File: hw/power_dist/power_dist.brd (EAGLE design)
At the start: 70 x 45 mm, 57 parts, among them J1 JST-ZH6SMT_VERT, J2 JST-PH4SMT_VERT, P1 XT30P, P2 XT30P, P3 XT30P, P4 XT30P, P5 XT30P, P6 XT30P, P7 XT90PW-M, Q1 TPH1R204PL, Q2 TPH1R204PL, Q3 TPH1R204PL, U1 ZXTR2012Z, U2 MAX150628TDFN, U3 STM32G474CEU6, U4 MIC4416, U5 MIC4416, U6 TCAN334G

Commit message: WIP of power_dist r4
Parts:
- removed D12, D3V3, DG, DI: PAD24AWG_PAD, precharge:24AWG_PAD
- removed D2: (no value), mfleds:LED0603
- removed D3: (no value), imu_junction:DO-214AB
- removed Q1, Q2, Q3: TPH1R204PL, imu_junction:SOP_ADVANCE
- added CR1: SMBJ51CA-E3/52, power_dist:DIODE_DO-214AC
- added MOSFET1, MOSFET2, MOSFET3: PSMN4R8-100BSEJ, power_dist:D2PAK_SOT404_NEX
- added R11, R12: 10k, mfpassives:R0603
- added R13: 15k 1%, mfpassives:R0603
- added U$5: JST-PH5VERT, power_dist:JST_B5B_PH-SM4-TB(LF)(SN)
- added U7: MF-DSC-SOT233-BSS138, mfdiscretesemi:SOT-23-3
- C1: value 1uF 50V -> 1uF
- C10, C11, C12, C13, C14, C3, C4: device mfpassives:C0402 -> mfpassives:C0603
- C5: value 0.1uF -> 0.01uF; device mfpassives:C0402 -> mfpassives:C0603
- C6: value 0.1uF -> 0.082uF; device mfpassives:C0402 -> mfpassives:C0603
- C7: value 10uF 50V -> 1uF; device mfpassives:C1206 -> mfpassives:C0603
- C8, C9: value 1uF 50V -> 1uF 100V; device mfpassives:C0603 -> mfpassives:C0805
- D1: value (none) -> MF-DIO-SOD123-1N4148; device mfleds:LED0603 -> mfdiscretesemi:SOD-123
- L1: value 33uH -> CBC3225T330KR; device mfpassives:L1210 -> power_dist:IND_TAIYO_CBC3225_TAY
- R1: value 220 -> 47k 1%
- R2: value 220 -> 15k 1%
- R4: value 10k 1% -> 4.7k 1%
- R5: value 100k 1% -> 0.3mOhm; device mfpassives:R0603 -> power_dist:SHUNT2512
- R6: value 10k 1% -> 24k 1%
- R7: value 10 1W -> 1k 1%; device mfpassives:R1206 -> mfpassives:R0603
- R8: value 100k 1% -> 10k
- R9: value 100k 1% -> 47k 1%
- U1: value ZXTR2012Z -> MAX15062AATA+T; device imu_junction:SOT89 -> power_dist:21-0487A_MXM
- U2: value MAX150628TDFN -> LM5066IPMHE/NOPB; device precharge:8TDFN -> power_dist:MXA28A_TEX
- U4: value MIC4416 -> FSV10150V; device imu_junction:SOT143 -> power_dist:TO277-3L_ONS
- U5: value MIC4416 -> MF-DSC-SOT233-MMBT3906; device imu_junction:SOT143 -> mfdiscretesemi:SOT-23-3
- moved U4 54.3 mm to (64.6, 3.60)
- moved C9 54.2 mm to (70.6, 3.60), turned to 270 degrees
- moved J1 53.3 mm to (16.0, 2.40), turned to 180 degrees
- moved L1 42.1 mm to (17.8, 46.4)
- moved C8 38.7 mm to (25.0, 44.8)
- moved U2 33.5 mm to (36.8, 31.4), turned to 270 degrees
- moved R2 30.3 mm to (36.4, 38.6), turned to 180 degrees
- moved R5 29.8 mm to (39.4, 41.8), turned to 0 degrees
- moved C7 29.4 mm to (36.5, 26.0)
- moved C15 29.2 mm to (25.2, 21.0), turned to 180 degrees
- moved C6 27.8 mm to (43.6, 23.7), turned to 180 degrees
- moved C3 27.8 mm to (19.2, 7.60), turned to 0 degrees
- moved R1 27.0 mm to (38.0, 37.2), turned to 180 degrees
- moved U5 26.7 mm to (43.4, 26.4)
- moved P3 25.2 mm to (68.0, 13.0), turned to 90 degrees
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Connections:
- removed net +12V: C2.P$1, C5.P$1, C6.P$1, D12.P$1, U1.3, U4.3, U5.3
- removed net +18V: C1.P$1, C8.P$1, D3.C, DI.P$1, P1.2, P2.2, P3.2, P4.2, P5.2, P6.2, P7.2, R3.P$2, U1.2, U1.PAD, U2.1, U2.2
- removed net FET_MAIN: R9.P$2, U3.9, U5.4
- removed net FET_PRECHARGE: R8.P$2, U3.8, U4.4
- removed net LX: L1.P$1, U2.8
- removed net PCHG: Q1.5, Q1.6, Q1.7, Q1.8, Q1.PAD, R7.P$1
- removed net V-OUT: D3.A, P1.1, P2.1, P3.1, P4.1, P5.1, P6.1, Q2.5, Q2.6, Q2.7, Q2.8, Q2.PAD, Q3.5, Q3.6, Q3.7, Q3.8, Q3.PAD, R5.P$2, R7.P$2
- removed net VSAMP_IN: R3.P$1, R4.P$2, U3.31
- removed net VSAMP_OUT: R5.P$1, R6.P$2, U3.30
- new net +24V: C8.P$1, CR1.1, P7.2, R1.P$1, R3.P$1, R5.1, R9.P$1, U1.1, U1.2, U2.5
- new net GPIO1: U$5.4, U3.39
- new net GPIO2: U$5.3, U3.40
- new net GPIO3: U$5.2, U3.41
- new net N$10: R6.P$1, U2.26
- new net N$11: C5.P$1, U2.25
- new net N$5: D1.ANODE, MOSFET1.1, MOSFET2.1, MOSFET3.1, R7.P$1, U2.2
- new net N$6: C7.P$1, U2.21
- new net N$9: R1.P$2, R2.P$1, U2.7, U7.P$3
- new net PGD: U2.28
- new net PSHDN: R13.P$1, R9.P$2, U3.26, U7.P$1
- new net SCL: R11.P$1, U2.13, U3.31
- new net SDA: R8.P$1, U2.11, U2.12, U3.30
- new net SMBA: R12.P$1, U2.14, U3.32
- new net VIN_SENSE: R3.P$2, R4.P$1, U2.8
- new net VSENSE_HIGH: R5.3, U2.4
- new net VSENSE_LOW: R5.4, U2.3
- new net VSWITCHED: C9.P$1, MOSFET1.3, MOSFET2.3, MOSFET3.3, P1.2, P2.2, P3.2, P4.2, P5.2, P6.2, U2.1, U4.3
- net CAN_SHDN: now also U3.27; no longer U3.32
- net GND: now also CR1.2, P1.1, P2.1, P3.1, P4.1, P5.1, P6.1, R13.P$2, R2.P$2, R4.P$2, R6.P$2, R7.P$2, U$5.5, U1.7, U2.10, U2.9, U4.2, U5.P$1, U7.P$2; no longer DG.P$1, Q1.1, Q1.2, Q1.3, Q2.1, Q2.2, Q2.3, Q3.1, Q3.2, Q3.3, R4.P$1, R6.P$1, R8.P$1, R9.P$1, U1.1, U2.7, U5.1
- net LED1: no longer D1.CATHODE
- net LED2: no longer D2.CATHODE
- net N$1: now also L1.2, U1.8; no longer D1.ANODE, R1.P$1
- net N$12: now also C6.P$1, U5.P$2; no longer Q1.4, U4.2
- net N$13: now also D1.CATHODE, U5.P$3; no longer C9.P$1, U2.3
- net N$3: now also MOSFET1.2, MOSFET2.2, MOSFET3.2, R5.2; no longer Q2.4, Q3.4, U5.2
- net N$4: now also C1.P$1, U1.3; no longer D2.ANODE, R2.P$1
- net VCC: now also C2.P$1, L1.1, R11.P$2, R12.P$2, R8.P$2, U$5.1, U1.4; no longer C7.P$1, D3V3.P$1, L1.P$2, R1.P$2, R2.P$2, U2.4
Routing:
- net +18V: track 60.3 -> 0.00 mm, vias 3 -> 0
- net FET_MAIN: track 59.7 -> 0.00 mm
- net FET_PRECHARGE: track 52.7 -> 0.00 mm
- net SWDIO: track 44.7 -> 0.00 mm
- net PWR_LED: track 43.3 -> 0.00 mm
- net GND: track 30.9 -> 0.00 mm, vias 58 -> 0
- net NRST: track 27.6 -> 0.00 mm
- net VSAMP_OUT: track 27.5 -> 0.00 mm, vias 2 -> 0
- net SWCLK: track 23.3 -> 0.00 mm
- net VCC: track 22.4 -> 0.00 mm, vias 22 -> 0
- net N$3: track 20.6 -> 0.00 mm, vias 2 -> 0
- net PWR_SW: track 19.2 -> 0.00 mm, vias 2 -> 0
- net N$12: track 18.8 -> 0.00 mm, vias 2 -> 0
- net VSAMP_IN: track 17.6 -> 0.00 mm, vias 2 -> 0
- net CAN_P: track 13.5 -> 0.00 mm
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- removed copper zone on layer 1, net +12V
- removed copper zone on layer 15, net +12V
- removed copper zone on layer 1, net +18V
- removed copper zone on layer 15, net +18V
- removed copper zone on layer 16, net +18V
- removed copper zone on layer 1, net GND
- removed copper zone on layer 2, net GND
- removed copper zone on layer 1, net LX
- removed copper zone on layer 1, net PCHG
- removed copper zone on layer 1, net V-OUT
- removed copper zone on layer 2, net V-OUT
- removed copper zone on layer 1, net VCC
- removed copper zone on layer 15, net VCC
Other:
- board size 70 x 45 mm -> 80 x 50 mm
- board text added: "power dist r4.0"
- board text removed: "+"
- board text removed: "-"
- board text removed: "12V"
- board text removed: "3V"
- board text removed: "GND"
- board text removed: "IN"
- board text removed: "power dist r3.1"

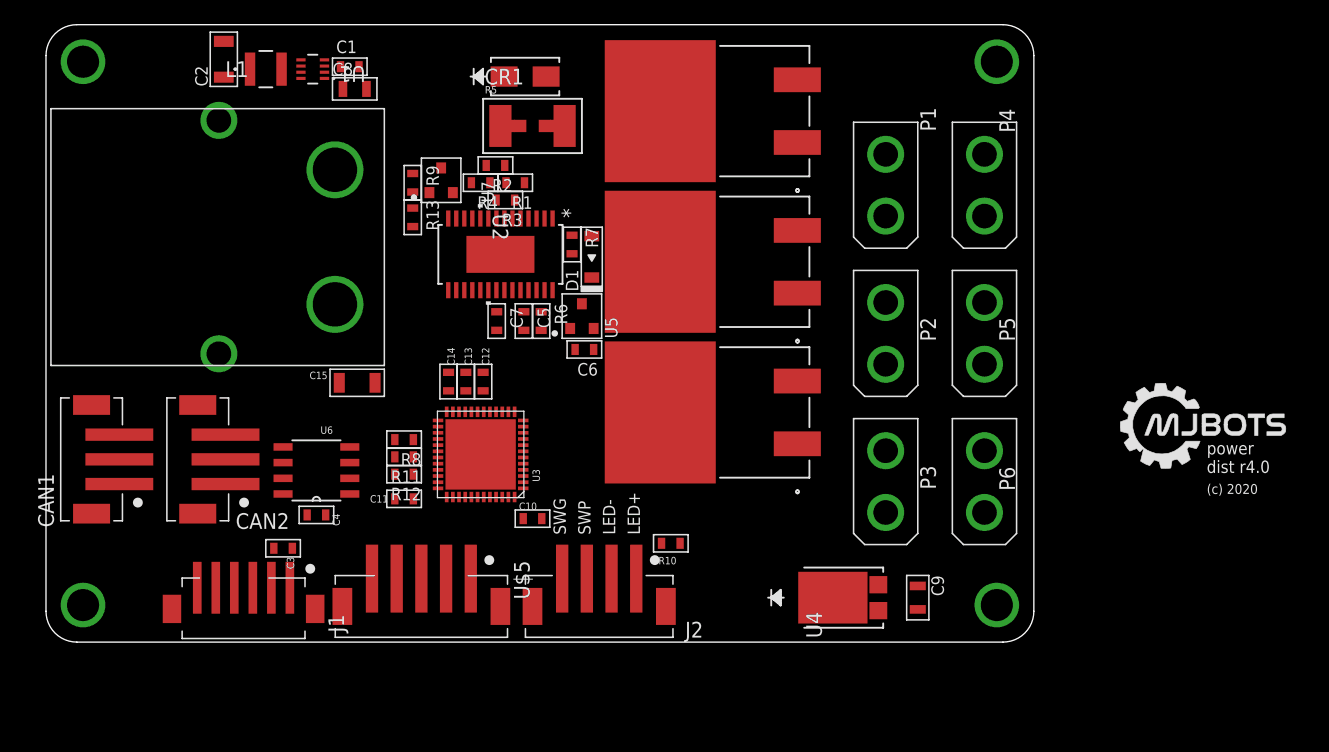
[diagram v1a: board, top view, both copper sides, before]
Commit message: power_dist r4 rough layout and most things renumbered
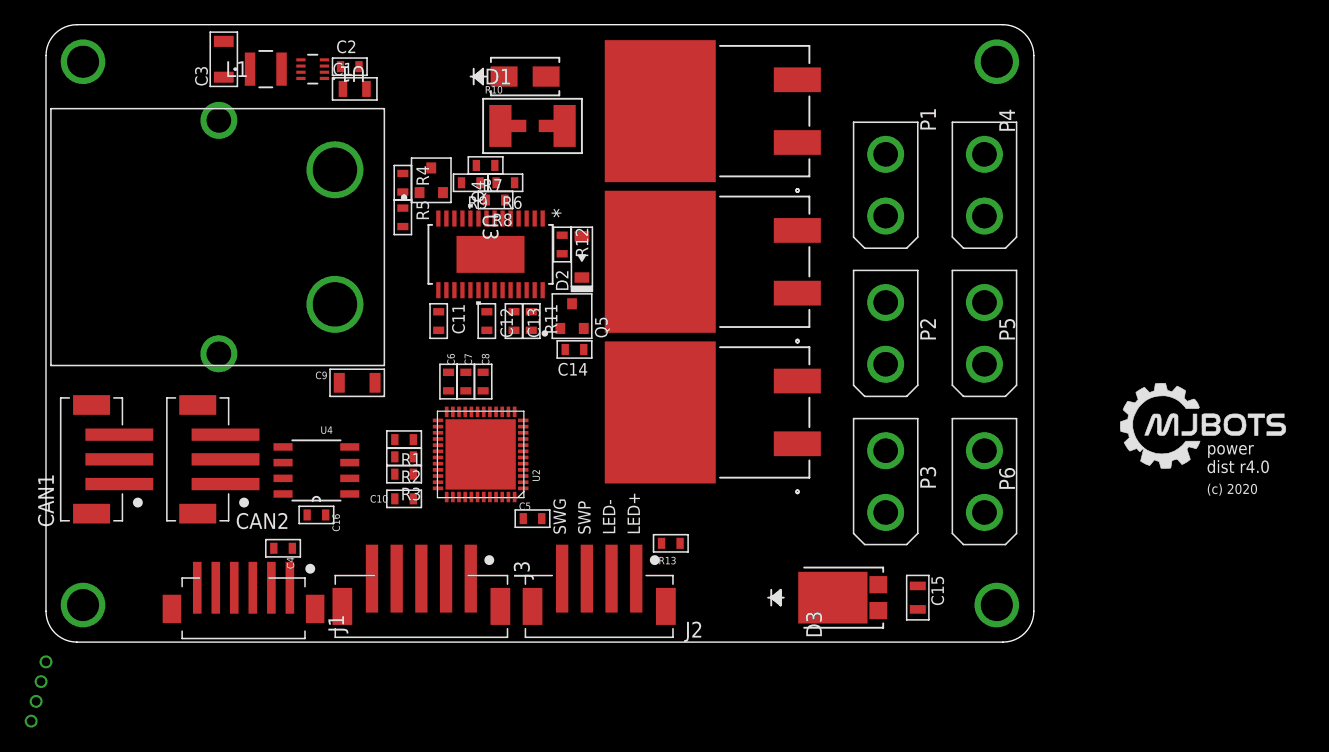
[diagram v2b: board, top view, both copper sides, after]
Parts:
- removed CR1: SMBJ51CA-E3/52, power_dist:DIODE_DO-214AC
- removed U5: MF-DSC-SOT233-MMBT3906, mfdiscretesemi:SOT-23-3
- removed U6: TCAN334G, precharge:SOIC8
- removed U7: MF-DSC-SOT233-BSS138, mfdiscretesemi:SOT-23-3
- added C16: 0.1uF, mfpassives:C0603
- added D2: MF-DIO-SOD123-1N4148, mfdiscretesemi:SOD-123
- added D3: FSV10150V, power_dist:TO277-3L_ONS
- added DB_3, DB_G, DB_VIN, DB_VSW: PAD24AWG_PAD, precharge:24AWG_PAD
- added Q4: MF-DSC-SOT233-BSS138, mfdiscretesemi:SOT-23-3
- added Q5: MF-DSC-SOT233-MMBT3906, mfdiscretesemi:SOT-23-3
- C1: value 1uF -> 1uF 100V; device mfpassives:C0603 -> mfpassives:C0805
- C11, C12: value 0.1uF -> 1uF
- C13: value 0.1uF -> 0.01uF
- C14: value 1uF -> 0.01uF
- C15: value 10uF 50V -> 1uF 100V; device mfpassives:C1206 -> mfpassives:C0805
- C2: value 10uF 50V -> 1uF; device mfpassives:C1206 -> mfpassives:C0603
- C3: value 0.1uF -> 10uF 50V; device mfpassives:C0603 -> mfpassives:C1206
- C5: value 0.01uF -> 0.1uF
- C6: value 0.082uF -> 1uF
- C7: value 1uF -> 0.1uF
- C8: value 1uF 100V -> 0.1uF; device mfpassives:C0805 -> mfpassives:C0603
- C9: value 1uF 100V -> 10uF 50V; device mfpassives:C0805 -> mfpassives:C1206
- D1: value MF-DIO-SOD123-1N4148 -> SMBJ51CA-E3/52; device mfdiscretesemi:SOD-123 -> power_dist:DIODE_DO-214AC
- R1: value 47k 1% -> 10k
- R10: value 220 -> 0.3mOhm; device mfpassives:R0603 -> power_dist:SHUNT2512
- R11: value 10k -> 24k 1%
- R12: value 10k -> 1k 1%
- R13: value 15k 1% -> 220
- R2: value 15k 1% -> 10k
- R3: value 100k 1% -> 10k
- R4: value 4.7k 1% -> 47k 1%
- R5: value 0.3mOhm -> 15k 1%; device power_dist:SHUNT2512 -> mfpassives:R0603
- R6: value 24k 1% -> 47k 1%
- R7: value 1k 1% -> 19.1k 1%
- R8: value 10k -> 140k 1%
- R9: value 47k 1% -> 6.49k 1%
- U2: value LM5066IPMHE/NOPB -> STM32G474CEU6; device power_dist:MXA28A_TEX -> precharge:QFN50P700X700X60-49N
- U3: value STM32G474CEU6 -> LM5066IPMHE/NOPB; device precharge:QFN50P700X700X60-49N -> power_dist:MXA28A_TEX
- U4: value FSV10150V -> TCAN334G; device power_dist:TO277-3L_ONS -> precharge:SOIC8
- moved C15 48.6 mm to (70.6, 3.60), turned to 270 degrees
- moved C9 48.6 mm to (25.2, 21.0), turned to 180 degrees
- moved U4 43.9 mm to (21.9, 13.9), turned to 180 degrees
- moved C3 39.9 mm to (14.4, 47.2), turned to 90 degrees
- moved R10 35.6 mm to (39.4, 41.8)
- moved R13 33.7 mm to (50.6, 8.00), turned to 0 degrees
- moved C8 25.9 mm to (35.4, 21.1), turned to 90 degrees
- moved R2 24.7 mm to (29.0, 15.0)
- moved R3 23.7 mm to (29.0, 13.6)
- moved R1 22.7 mm to (29.0, 16.4)
- moved R12 22.6 mm to (41.8, 32.2), turned to 270 degrees
- moved R8 20.8 mm to (36.4, 35.8)
- moved U2 16.3 mm to (35.2, 15.2), turned to 180 degrees
- moved U3 16.2 mm to (36.0, 31.4), turned to 270 degrees
- moved C5 16.0 mm to (39.4, 10.0), turned to 0 degrees
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- renumbered MOSFET1 to Q1, MOSFET2 to Q2, MOSFET3 to Q3, U$5 to J3
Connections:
- new net N$7: C11.P$1, U3.15
- net +24V: now also C1.P$1, D1.1, DB_VIN.P$1, R10.1, R4.P$1, R6.P$1, R8.P$1, U3.5; no longer C8.P$1, CR1.1, R1.P$1, R3.P$1, R5.1, R9.P$1, U2.5
- net CAN_N: now also U4.6; no longer U6.6
- net CAN_P: now also U4.7; no longer U6.7
- net CAN_RX: now also U2.33, U4.4; no longer U3.33, U6.4
- net CAN_SHDN: now also U2.27, U4.5; no longer U3.27, U6.5
- net CAN_TX: now also U2.34, U4.1; no longer U3.34, U6.1
- net GND: now also C16.P$2, D1.2, D3.1, D3.2, DB_G.P$1, Q4.P$2, Q5.P$1, R11.P$2, R12.P$2, R5.P$2, R9.P$2, U2.29, U2.49, U3.10, U3.9, U4.8; no longer CR1.2, R13.P$2, R2.P$2, R4.P$2, R6.P$2, U2.10, U2.9, U3.49, U4.1, U5.P$1, U6.2, U6.8, U7.P$2
- net GPIO1: now also U2.39; no longer U3.39
- net GPIO2: now also U2.40; no longer U3.40
- net GPIO3: now also U2.41; no longer U3.41
- net LED1: now also U2.47; no longer U3.47
- net LED2: now also U2.45; no longer U3.45
- net N$10: now also R11.P$1, U3.26; no longer R6.P$1, U2.26
- net N$11: now also C13.P$1, U3.25; no longer C5.P$1, U2.25
- net N$12: now also C14.P$1, Q5.P$2; no longer C6.P$1, U5.P$2
- net N$13: now also D2.CATHODE, Q5.P$3; no longer D1.CATHODE, U5.P$3
- net N$2: now also R13.P$1; no longer R10.P$1
- net N$3: now also R10.2; no longer R5.2
- net N$4: now also C2.P$1; no longer C1.P$1
- net N$5: now also D2.ANODE, R12.P$1, U3.2; no longer D1.ANODE, R7.P$1, U2.2
- net N$6: now also C12.P$1, U3.21; no longer C7.P$1, U2.21
- net N$9: now also Q4.P$3, R6.P$2, R7.P$1, U3.7; no longer R1.P$2, R2.P$1, U2.7, U7.P$3
- net NRST: now also C4.P$1, U2.7; no longer C3.P$1, U3.7
- net PGD: now also U3.28; no longer U2.28
- net PSHDN: now also Q4.P$1, R4.P$2, R5.P$1, U2.26; no longer R13.P$1, R9.P$2, U3.26, U7.P$1
- net PWR_LED: now also U2.10; no longer U3.10
- net PWR_SW: now also U2.11; no longer U3.11
- net SCL: now also R2.P$1, U2.31, U3.13; no longer R11.P$1, U2.13, U3.31
- net SDA: now also R1.P$1, U2.30, U3.11, U3.12; no longer R8.P$1, U2.11, U2.12, U3.30
- net SMBA: now also R3.P$1, U2.32, U3.14; no longer R12.P$1, U2.14, U3.32
- net SWCLK: now also U2.37; no longer U3.37
- net SWDIO: now also U2.36; no longer U3.36
- net VCC: now also C16.P$1, C3.P$1, C5.P$1, C6.P$1, C7.P$1, C8.P$1, C9.P$1, DB_3.P$1, R1.P$2, R13.P$2, R2.P$2, R3.P$2, U2.1, U2.20, U2.21, U2.23, U2.35, U2.48, U4.3; no longer C11.P$1, C12.P$1, C13.P$1, C14.P$1, C15.P$1, C2.P$1, C4.P$1, R10.P$2, R11.P$2, R12.P$2, R8.P$2, U3.1, U3.20, U3.21, U3.23, U3.35, U3.48, U6.3
- net VIN_SENSE: now also R8.P$2, R9.P$1, U3.8; no longer R3.P$2, R4.P$1, U2.8
- net VSENSE_HIGH: now also R10.3, U3.4; no longer R5.3, U2.4
- net VSENSE_LOW: now also R10.4, U3.3; no longer R5.4, U2.3
- net VSWITCHED: now also C15.P$1, D3.3, DB_VSW.P$1, U3.1; no longer C9.P$1, U2.1, U4.3

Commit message: WIP checkpoint of power_dist r4
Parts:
- added D4, D5: (no value), mfleds:LED0603
- added R14, R15: 220, mfpassives:R0603
- moved C15 9.25 mm to (63.4, 9.40)
- moved D3 8.64 mm to (58.2, 9.40)
- moved R1 1.34 mm to (28.4, 17.6)
- moved R2 1.17 mm to (28.4, 16.0)
- moved R3 1.00 mm to (28.4, 14.4)
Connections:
- new net N$14: D5.ANODE, R15.P$1
- new net N$8: D4.ANODE, R14.P$1
- net LED1: now also D4.CATHODE, U2.8; no longer U2.47
- net LED2: now also D5.CATHODE, U2.9; no longer U2.45
- net VCC: now also R14.P$2, R15.P$2

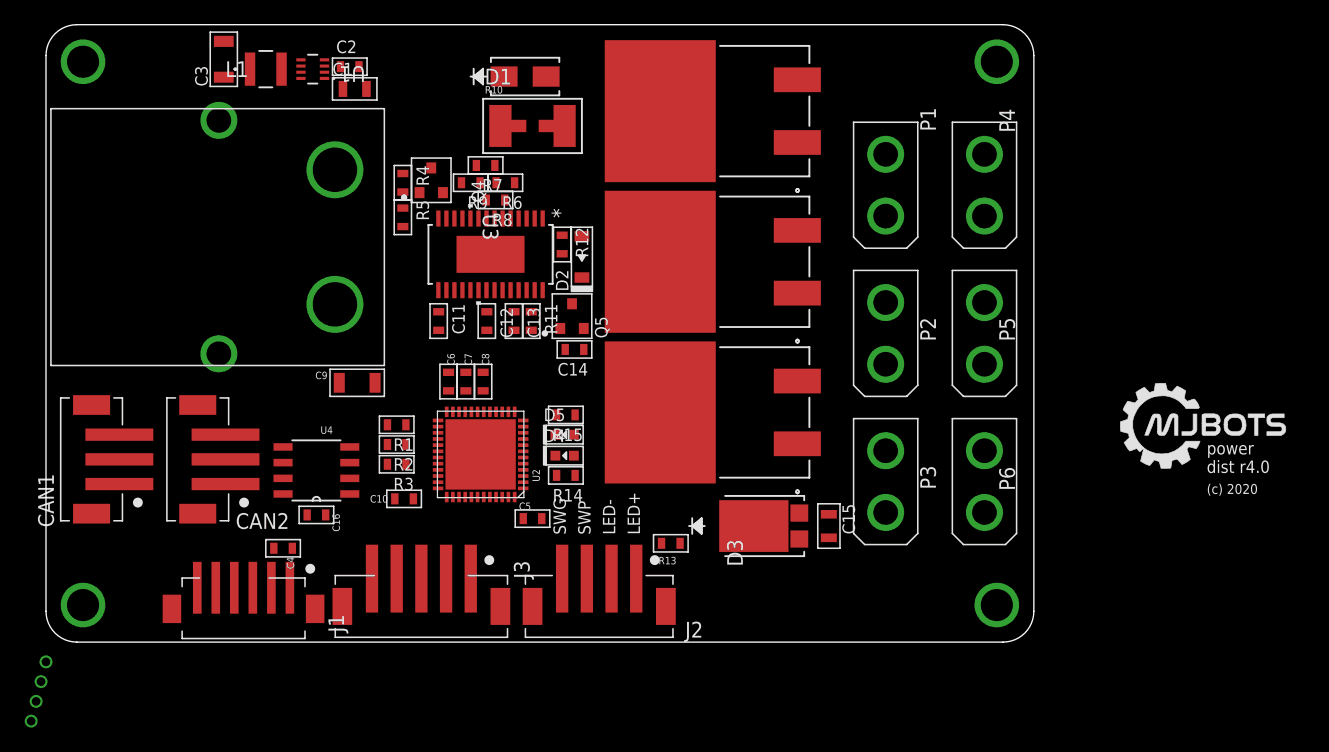
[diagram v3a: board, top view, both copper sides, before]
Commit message: power_dist r4: Checkpoint, most power/gnd routed
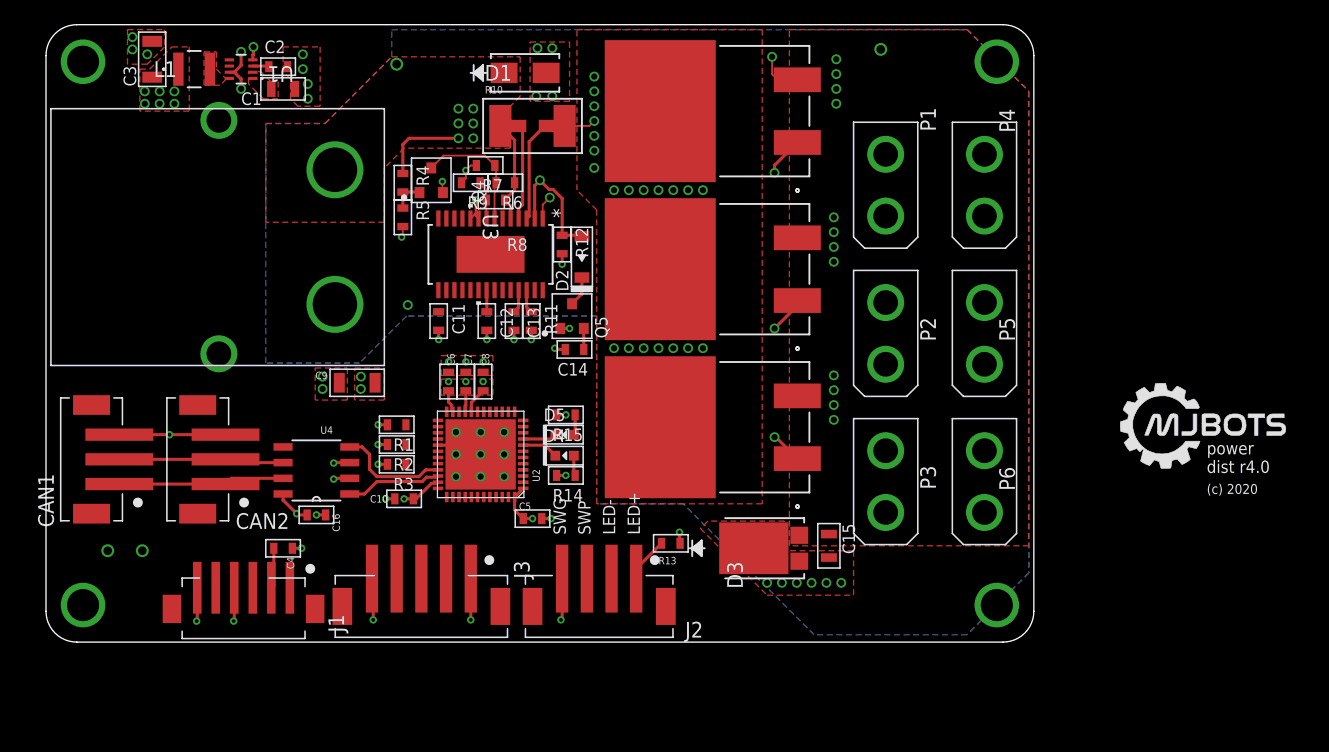
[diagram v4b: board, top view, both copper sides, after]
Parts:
- moved DB_VSW 86.4 mm to (67.6, 48.0)
- moved DB_VIN 57.7 mm to (28.4, 46.8)
- moved DB_3 15.1 mm to (5.00, 7.40)
- moved DB_G 11.9 mm to (7.80, 7.40)
- moved C1 5.80 mm to (19.2, 44.8)
- moved C2 5.80 mm to (18.8, 46.6)
- moved C3 5.80 mm to (8.60, 47.2)
- moved L1 5.80 mm to (12.0, 46.4)
- moved U1 5.80 mm to (15.8, 46.4)
- moved D3 1.80 mm to (58.2, 7.60)
- moved C15 1.60 mm to (63.4, 7.80)
- moved Q2 1.20 mm to (54.0, 17.4)
- moved Q1 0.60 mm to (54.0, 30.2)
- moved D1 0.30 mm to (38.8, 46.1)
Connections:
- net N$3 renamed VIN_POST
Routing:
- net N$5: track 0.00 -> 80.9 mm, vias 0 -> 4
- net GND: track 0.00 -> 43.0 mm, vias 0 -> 54
- net VSWITCHED: track 0.00 -> 35.7 mm, vias 0 -> 14
- net VCC: track 0.00 -> 26.6 mm, vias 0 -> 24
- net +24V: track 0.00 -> 15.6 mm, vias 0 -> 6
- net CAN_P: track 0.00 -> 13.5 mm
- net CAN_N: track 0.00 -> 13.4 mm
- net N$9: track 0.00 -> 10.3 mm
- net CAN_RX: track 0.00 -> 9.08 mm
- net VSENSE_LOW: track 0.00 -> 8.11 mm
- net CAN_TX: track 0.00 -> 7.75 mm
- net VSENSE_HIGH: track 0.00 -> 7.72 mm
- net VIN_POST: track 0.00 -> 4.58 mm, vias 0 -> 21
- net N$2: track 0.00 -> 3.71 mm
- net NRST: track 0.00 -> 3.28 mm
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- added copper zone on layer 1, net +24V
- added copper zone on layer 15, net +24V
- added copper zone on layer 1, net GND
- added copper zone on layer 16, net GND
- added copper zone on layer 2, net GND
- added copper zone on layer 1, net N$1
- added copper zone on layer 1, net VCC
- added copper zone on layer 15, net VCC
- added copper zone on layer 1, net VIN_POST
- added copper zone on layer 15, net VIN_POST
- added copper zone on layer 1, net VSWITCHED
- added copper zone on layer 15, net VSWITCHED
